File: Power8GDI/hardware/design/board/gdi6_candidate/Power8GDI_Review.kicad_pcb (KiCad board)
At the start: 4 copper layers, 245 x 165 mm, 1092 parts, among them J101 SWD 3V3 target reference, J1501 Molex 1050170001, J1502 Molex 1040310811, J5600 Conn_02x03_Odd_Even, J601 6437288-1 / KEY1 CANDIDATE, J602 6437288-1 / KEY1 CANDIDATE, J603 6437288-1 / KEY1 CANDIDATE, J604 6437288-1 / KEY1 CANDIDATE, Q1510 2N7002,215, Q201 IPD60N10S4L12ATMA1, Q202 IPD60N10S4L12ATMA1, Q203 IPD60N10S4L12ATMA1, Q204 IPD60N10S4L12ATMA1, Q205 IPD60N10S4L12ATMA1, Q206 IPD60N10S4L12ATMA1, Q207 IPD60N10S4L12ATMA1, Q208 IPD60N10S4L12ATMA1, Q209 IPD60N10S4L12ATMA1, Q211 IPD60N10S4L12ATMA1, Q212 IPD60N10S4L12ATMA1, Q213 IPD60N10S4L12ATMA1, Q301 IPD60N10S4L12ATMA1, Q302 IPD60N10S4L12ATMA1, Q303 IPD60N10S4L12ATMA1, Q304 IPD60N10S4L12ATMA1, Q305 IPD60N10S4L12ATMA1, Q306 IPD60N10S4L12ATMA1, Q307 IPD60N10S4L12ATMA1, Q308 IPD60N10S4L12ATMA1, Q309 IPD60N10S4L12ATMA1, Q311 IPD60N10S4L12ATMA1, Q312 IPD60N10S4L12ATMA1, Q313 IPD60N10S4L12ATMA1, Q5001 IPD90N10S4-06, Q5002 IPD90N10S4-06, Q5051 IPD90N10S4-06, Q5052 IPD90N10S4-06, Q5420 STGB18N40LZT4, Q5440 STGB18N40LZT4, Q5460 STGB18N40LZT4, Q5480 STGB18N40LZT4, Q5500 STGB18N40LZT4, Q5520 STGB18N40LZT4, Q5600 VND7NV04TR-E, Q5620 BC847B-QR, Q6200 IPD90N10S4-06, Q6201 IPD90N10S4-06, Q6250 IPD90N10S4-06, Q6251 IPD90N10S4-06, U101 STM32F767IIT6, U103 TCAN1042HGVDRQ1, U104 TLIN1029ADRQ1, U1101 TLE9104SHXUMA1, U1102 TLE9104SHXUMA1, U1103 TLE9104SHXUMA1, U1104 TLE9104SHXUMA1, U1105 TLE9104SHXUMA1, U1106 TLE9104SHXUMA1, U1121 SN74LVC14AQPWRQ1, U1122 SN74LVC14AQPWRQ1, U1123 SN74LVC14AQPWRQ1, U1124 SN74LVC14AQPWRQ1, U1125 SN74LVC14AQPWRQ1, U1126 SN74LVC14AQPWRQ1, U1140 SN74LVC1G17QDBVRQ1, U1501 TCAN1042HGVDRQ1, U1502 TLIN1029ADRQ1, U1530 TPS7B4253QDDARQ1, U1531 TPS7B4253QDDARQ1, U1600 SN74LVC14AQPWRQ1, U1701 TPIC8101DWR, U1702 SN74AHCT244QPWRQ1, U1703 CLVC1G125QDBVRQ1, U201 MC33PT2001AE, U249 NCV78M05ABDTRKG, U301 MC33PT2001AE, U349 NCV78M05ABDTRKG, U5001 LM74800QDRRRQ1, U5051 LM74800QDRRRQ1, U5101 SN74LVC2G08QDCURQ1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

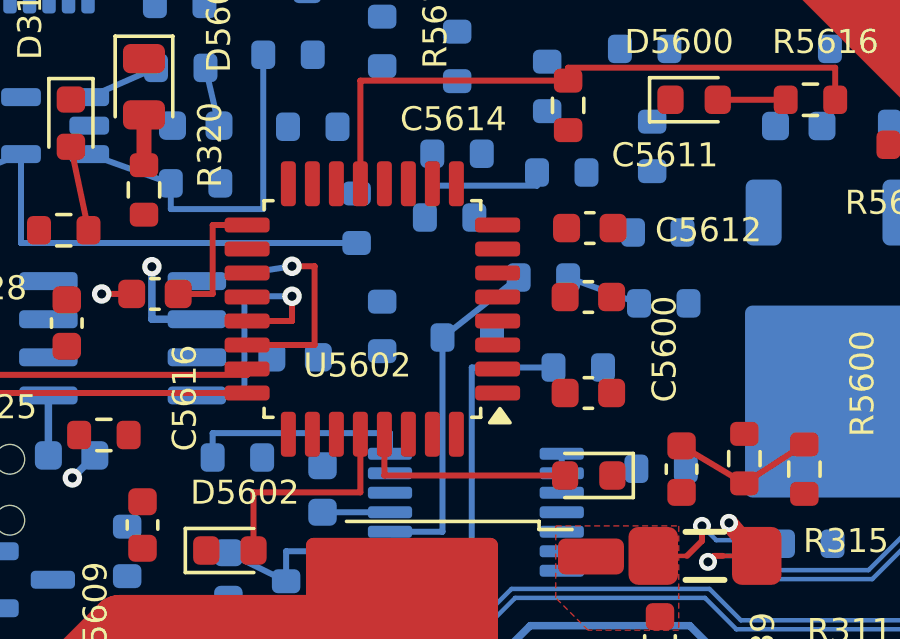
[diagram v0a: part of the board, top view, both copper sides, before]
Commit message: Connect GDI6 WBO MCU and bypass ground returns
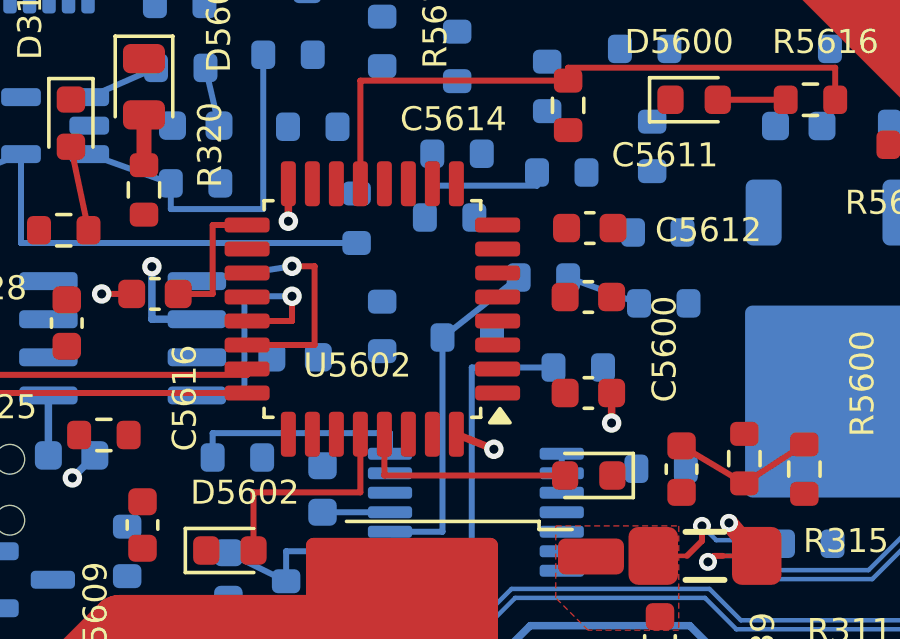
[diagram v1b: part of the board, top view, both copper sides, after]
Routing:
- net GND: track 112.7 -> 116.3 mm, vias 52 -> 55
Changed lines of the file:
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@@
+	)
+	(segment
+		(start 174.97795 68.35)
+		(end 176.22795 68.85)
+		(width 0.25)
+		(layer "F.Cu")
+		(net 133)
 	)
 	(segment
@@
 	)
 	(segment
+		(start 169.37795 60)
+		(end 169.37795 61.25)
+		(width 0.25)
+		(layer "F.Cu")
+		(net 133)
+	)
+	(segment
 		(start 11.55 112.25)
 		(end 10.45 112.25)
@@
 	)
 	(segment
+		(start 180.15295 66.975)
+		(end 180.15295 67.975)
+		(width 0.25)
+		(layer "F.Cu")
+		(net 133)
+	)
+	(segment
 		(start 61.525 81.18998)
 		(end 61.525 82.29048)
@@
 	)
 	(via
+		(at 169.37795 61.25)
+		(size 0.65)
+		(drill 0.3)
+		(layers "F.Cu" "B.Cu")
+		(net 133)
+	)
+	(via
 		(at 33.7 41.85)
 		(size 0.6)
@@
 	(via
 		(at 178.8625 81.8)
+		(size 0.65)
+		(drill 0.3)
+		(layers "F.Cu" "B.Cu")
+		(net 133)
+	)
+	(via
+		(at 180.15295 67.975)
 		(size 0.65)
 		(drill 0.3)
@@
 		(drill 0.3)
 		(layers "F.Cu" "B.Cu")
+		(net 133)
+	)
+	(via
+		(at 176.22795 68.85)
+		(size 0.65)
+		(drill 0.3)
+		(layers "F.Cu" "B.Cu")

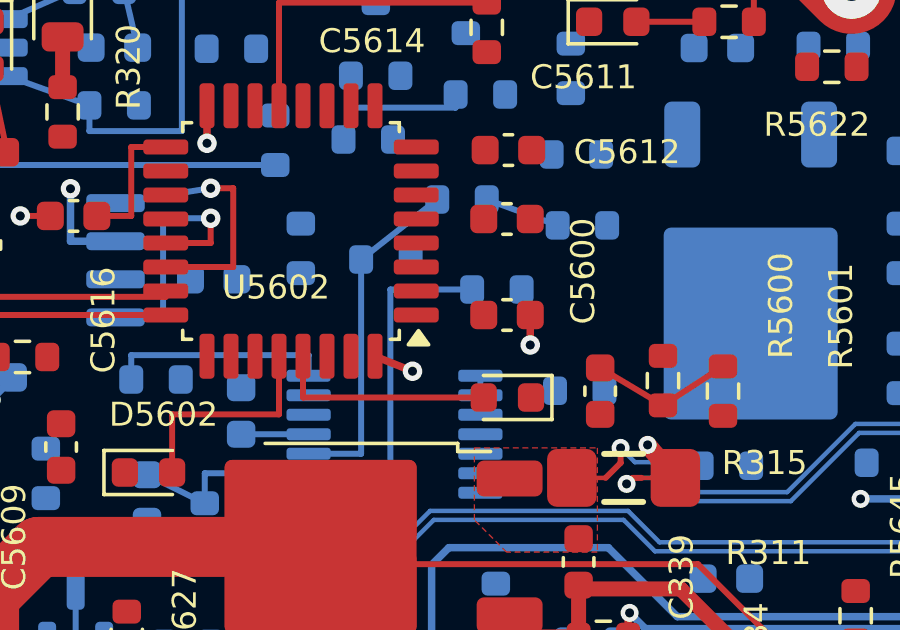
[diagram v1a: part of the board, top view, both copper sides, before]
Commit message: Route GDI6 WBO MCU VDD bypass connection
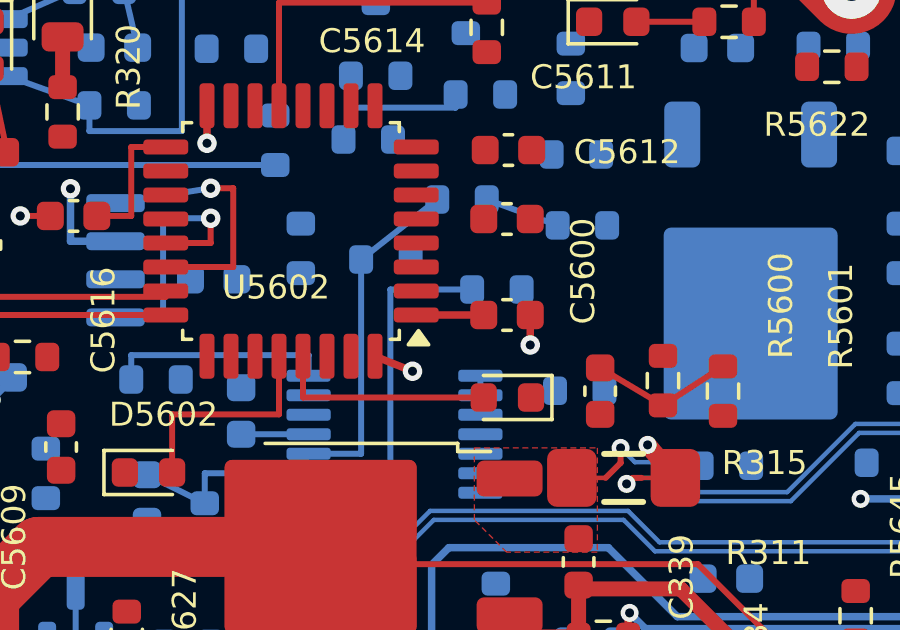
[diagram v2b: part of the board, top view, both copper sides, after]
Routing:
- net WBO1_3V3: track 13.8 -> 16.1 mm
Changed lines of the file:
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@@
+	)
+	(segment
+		(start 176.35295 66.975)
+		(end 178.60295 66.975)
+		(width 0.25)
+		(layer "F.Cu")
+		(net 632)
 	)
 	(segment
